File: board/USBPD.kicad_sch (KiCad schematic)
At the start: 22 parts

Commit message: pcb
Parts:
- removed J?: ISP, symbol Connector_Generic:Conn_02x03_Odd_Even
- removed J?: UART, symbol Connector:Conn_01x06_Female
- removed Q? (x2): PMOS, symbol Device:Q_PMOS_DGS
- removed R?: 10k, symbol Device:R
- removed U?: ATmega328-M, Package_DFN_QFN:QFN-32-1EP_5x5mm_P0.5mm_EP3.1x3.1mm, symbol MCU_Microchip_ATmega:ATmega328-M
- added J3: UDPI, Jumper:SolderJumper-3_P1.3mm_Open_RoundedPad1.0x1.5mm_NumberLabels, symbol Connector:Conn_01x03_Female
- added J4: UART, Connector_Molex:Molex_PicoBlade_53047-0410_1x04_P1.25mm_Vertical, symbol Connector:Conn_01x04_Female
- added Q1, Q3: PMOS, Package_TO_SOT_SMD:SOT-23-6, symbol Device:Q_PMOS_DGS
- added R3: 10k, Resistor_SMD:R_0603_1608Metric, symbol Device:R
- added U3: ATtiny1626-M, Package_DFN_QFN:VQFN-20-1EP_3x3mm_P0.4mm_EP1.7x1.7mm, symbol MCU_Microchip_ATtiny:ATtiny1626-M
- C1, C2, C3: renamed from C?; footprint (none) -> Capacitor_SMD:C_0603_1608Metric
- D1: renamed from D?; footprint (none) -> Package_TO_SOT_SMD:SOT-23
- D2, D4: renamed from D?; footprint (none) -> LED_SMD:LED_0603_1608Metric
- D3: renamed from D?; value D -> D_POW; footprint (none) -> Package_TO_SOT_SMD:SOT-23
- J1: renamed from J?; footprint (none) -> Connector_USB:USB_C_Receptacle_GCT_USB4085
- J2: renamed from J?; footprint (none) -> Connector_PinHeader_2.54mm:PinHeader_1x04_P2.54mm_Vertical
- Q2: renamed from Q?; footprint (none) -> Package_TO_SOT_SMD:SOT-23-6
- R1, R2, R4, R5: renamed from R?; footprint (none) -> Resistor_SMD:R_0603_1608Metric
- gave numbers to parts that had none: 2
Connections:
- net +3.3V: now also J3.3 (Pin_3), J4.1 (Pin_1), U3.4 (VCC)
- net +5V: now also Q3.1 (D), Q3.2 (D), Q3.5 (D), Q3.6 (D)
- net GND: now also J3.2 (Pin_2), J4.4 (Pin_4), U3.21 (GND), U3.3 (GND)
- net RTS: now also J3.1 (Pin_1), U3.19 (~{RESET}/PA0)
- net RX: now also J4.3 (Pin_3), U3.12 (PB2)
- net SNK: now also Q1.3 (G), U3.16 (PC1)
- net TX: now also J4.2 (Pin_2), U3.11 (PB3)
- net VCC: now also Q2.2 (D), Q2.5 (D), Q2.6 (D), Q1.4 (S)
- net at R1.2, U2.10 (CC1), U2.11 (CC1): now also D1.3 (K); no longer D1.2 (K)
- net SRC: now reaches Q2.3 (G)
- net SRC: now also Q3.3 (G), R3.2, U3.15 (PC0)
- net at R2.2, U2.1 (CC2), U2.14 (CC2): now also D1.2 (K); no longer D1.3 (K)
- net at U2.5 (INT_N): now also U3.10 (PB4)
- net at U2.6 (SCL): now also U3.14 (PB0)
- net at U2.7 (SDA): now also U3.13 (PB1)
- net at J2.1 (Pin_1): now also Q1.1 (D), Q1.2 (D), Q1.5 (D), Q1.6 (D)
- net at R5.2: now also U3.18 (PC3)
- net at R4.2: now also U3.17 (PC2)
- new net: Q2.4 (S), Q3.4 (S), R3.1
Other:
- moved on the sheet: D2, D4, R4, R5

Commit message: update pcb
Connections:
- net GND: now also D1.3 (A); no longer D1.1 (A)
- net at R1.2, U2.10 (CC1), U2.11 (CC1): now also D1.1 (K); no longer D1.3 (K)
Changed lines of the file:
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@@
   (symbol (lib_id "Device:D_Dual_CommonAnode_AKK_Parallel") (at 89.535 133.985 90) (unit 1)
     (in_bom yes) (on_board yes)
-    (property "Reference" "D1" (id 0) (at 88.265 132.715 90)
+    (property "Reference" "D1" (id 0) (at 88.265 135.255 90)
       (effects (font (size 1.27 1.27)) (justify right))
     )
-    (property "Value" "DUAL_SCH" (id 1) (at 84.455 130.175 0)
+    (property "Value" "DUAL_SCH" (id 1) (at 85.725 139.065 0)
       (effects (font (size 1.27 1.27)) (justify right))
     )
-    (property "Footprint" "Package_TO_SOT_SMD:SOT-23" (id 2) (at 89.535 135.255 0)
+    (property "Footprint" "Package_TO_SOT_SMD:SOT-23" (id 2) (at 90.805 133.985 0)
       (effects (font (size 1.27 1.27)) hide)
     )
-    (property "Datasheet" "~" (id 3) (at 89.535 135.255 0)
+    (property "Datasheet" "~" (id 3) (at 90.805 133.985 0)
       (effects (font (size 1.27 1.27)) hide)
     )
+    (pin "3")
+    (pin "2")
     (pin "1")
-    (pin "2")
-    (pin "3")
   )
   (sheet_instances

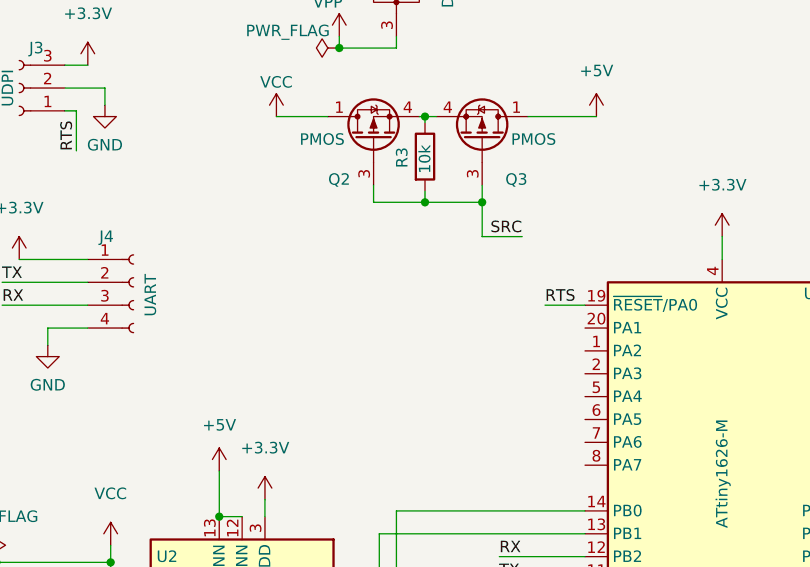
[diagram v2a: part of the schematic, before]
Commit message: use LVL translator for switch
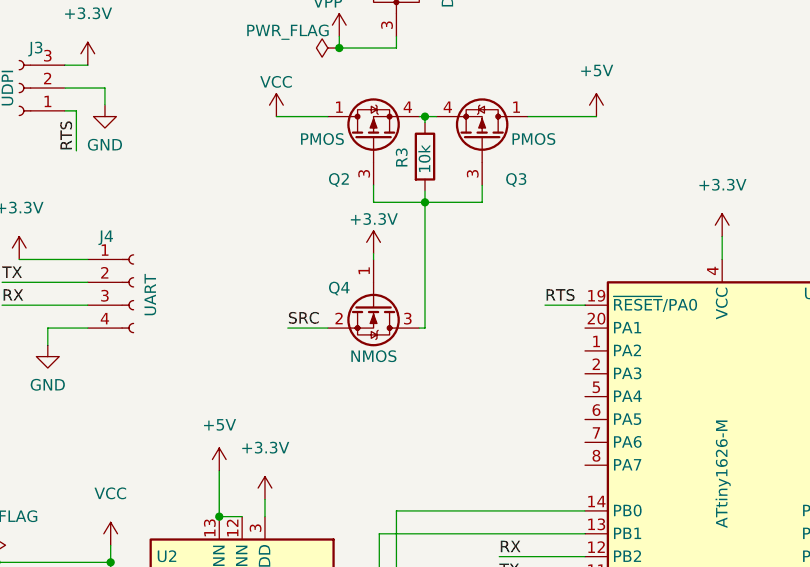
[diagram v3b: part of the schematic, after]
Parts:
- added Q4: NMOS, Package_TO_SOT_SMD:SOT-23, symbol Device:Q_NMOS_GSD
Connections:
- net +3.3V: now also Q4.1 (G)
- net SRC: now also Q4.2 (S); no longer Q2.3 (G), Q3.3 (G), R3.2
- new net: Q2.3 (G), Q3.3 (G), Q4.3 (D), R3.2
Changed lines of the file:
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@@
   (junction (at 80.645 45.72) (diameter 0) (color 0 0 0 0)
   )
-  (junction (at 133.985 78.105) (diameter 0) (color 0 0 0 0)
-  )
   (wire (pts (xy 145.415 122.555) (xy 127.635 122.555))
     (stroke (width 0) (type default) (color 0 0 0 0))
@@
     (stroke (width 0) (type default) (color 0 0 0 0))
   )
+  (wire (pts (xy 127 92.075) (xy 127.635 92.075))
+    (stroke (width 0) (type default) (color 0 0 0 0))
+  )
   (wire (pts (xy 66.04 52.705) (xy 66.04 55.245))
     (stroke (width 0) (type default) (color 0 0 0 0))
@@
     (stroke (width 0) (type default) (color 0 0 0 0))
   )
+  (wire (pts (xy 127.635 78.105) (xy 127.635 92.075))
+    (stroke (width 0) (type default) (color 0 0 0 0))
+  )
   (wire (pts (xy 121.92 78.105) (xy 127.635 78.105))
     (stroke (width 0) (type default) (color 0 0 0 0))
@@
     (stroke (width 0) (type default) (color 0 0 0 0))
   )
-  (wire (pts (xy 133.985 81.915) (xy 138.43 81.915))
+  (wire (pts (xy 116.84 92.075) (xy 112.395 92.075))
     (stroke (width 0) (type default) (color 0 0 0 0))
   )
@@
     (stroke (width 0) (type default) (color 0 0 0 0))
   )
-  (wire (pts (xy 133.985 78.105) (xy 133.985 81.915))
-    (stroke (width 0) (type default) (color 0 0 0 0))
-  )
   (wire (pts (xy 183.515 120.015) (xy 175.895 120.015))
     (stroke (width 0) (type default) (color 0 0 0 0))
@@
   )
   (wire (pts (xy 80.645 45.72) (xy 95.25 45.72))
+    (stroke (width 0) (type default) (color 0 0 0 0))
+  )
+  (wire (pts (xy 121.92 83.82) (xy 121.92 84.455))
     (stroke (width 0) (type default) (color 0 0 0 0))
   )
@@
     (effects (font (size 1.27 1.27)) (justify left bottom))
   )
-  (label "SRC" (at 138.43 81.915 180)
-    (effects (font (size 1.27 1.27)) (justify right bottom))
+  (label "SRC" (at 112.395 92.075 0)
+    (effects (font (size 1.27 1.27)) (justify left bottom))
   )
   (label "SNK" (at 182.245 114.935 180)
@@
     (pin "1")
   )
+  (symbol (lib_id "power:+3.3V") (at 121.92 83.82 0) (unit 1)
+    (in_bom yes) (on_board yes)
+    (property "Reference" "#PWR0101" (id 0) (at 121.92 87.63 0)
+      (effects (font (size 1.27 1.27)) hide)
+    )
+    (property "Value" "+3.3V" (id 1) (at 121.92 80.01 0))
+    (property "Footprint" "" (id 2) (at 121.92 83.82 0)
+      (effects (font (size 1.27 1.27)) hide)
+    )
+    (property "Datasheet" "" (id 3) (at 121.92 83.82 0)
+      (effects (font (size 1.27 1.27)) hide)
+    )
+    (pin "1")
+  )
   (symbol (lib_id "power:GND") (at 99.695 45.72 0) (unit 1)
     (in_bom yes) (on_board yes) (fields_autoplaced)
@@
     )
     (pin "1")
+  )
+  (symbol (lib_id "Device:Q_NMOS_GSD") (at 121.92 89.535 270) (unit 1)
+    (in_bom yes) (on_board yes)
+    (property "Reference" "Q4" (id 0) (at 118.11 87.63 90))
+    (property "Value" "NMOS" (id 1) (at 121.92 95.25 90))
+    (property "Footprint" "Package_TO_SOT_SMD:SOT-23" (id 2) (at 124.46 94.615 0)
+      (effects (font (size 1.27 1.27)) hide)
+    )
+    (property "Datasheet" "~" (id 3) (at 121.92 89.535 0)
+      (effects (font (size 1.27 1.27)) hide)
+    )
+    (pin "1")
+    (pin "2")
+    (pin "3")
   )
   (symbol (lib_id "power:+3.3V") (at 109.855 111.125 0) (unit 1)
@@
       (effects (font (size 1.27 1.27)) hide)
     )
+    (pin "1")
+    (pin "2")
     (pin "3")
-    (pin "2")
-    (pin "1")
   )
   (sheet_instances
@@
       (reference "#PWR024") (unit 1) (value "+3.3V") (footprint "")
     )
+    (path "/a0f2d135-a950-4986-914a-14e9240a5839"
+      (reference "#PWR0101") (unit 1) (value "+3.3V") (footprint "")
+    )
     (path "/155bc465-7c5b-4ad8-a0b7-7a4fa179603d"
       (reference "C1") (unit 1) (value "0.1u") (footprint "Capacitor_SMD:C_0603_1608Metric")
@@
       (reference "Q3") (unit 1) (value "PMOS") (footprint "Package_TO_SOT_SMD:SOT-23-6")
     )
+    (path "/e43741df-ef2f-4609-8af9-80683406fbfc"
+      (reference "Q4") (unit 1) (value "NMOS") (footprint "Package_TO_SOT_SMD:SOT-23")
+    )
     (path "/0788e7e5-aa18-419c-88ac-24635c3a4dee"
